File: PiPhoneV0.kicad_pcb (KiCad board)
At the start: 2 copper layers, 70.5 x 117.5 mm, 50 parts, among them J1 GPIO, J2 TL040WVS03-H1263A, J3 Conn_01x15_MountingPin, SW1 SW_Push, SW10 SW_Push, SW11 SW_Push, SW12 SW_Push, SW13 SW_Push, SW14 SW_Push, SW15 SW_Push, SW16 SW_Push, SW17 SW_Push, SW18 SW_Push, SW2 SW_Push, SW3 SW_Push, SW4 SW_Push, SW5 SW_Push, SW6 SW_Push, SW7 SW_Push, SW8 SW_Push, SW9 SW_Push, U2 TPS61165DRV

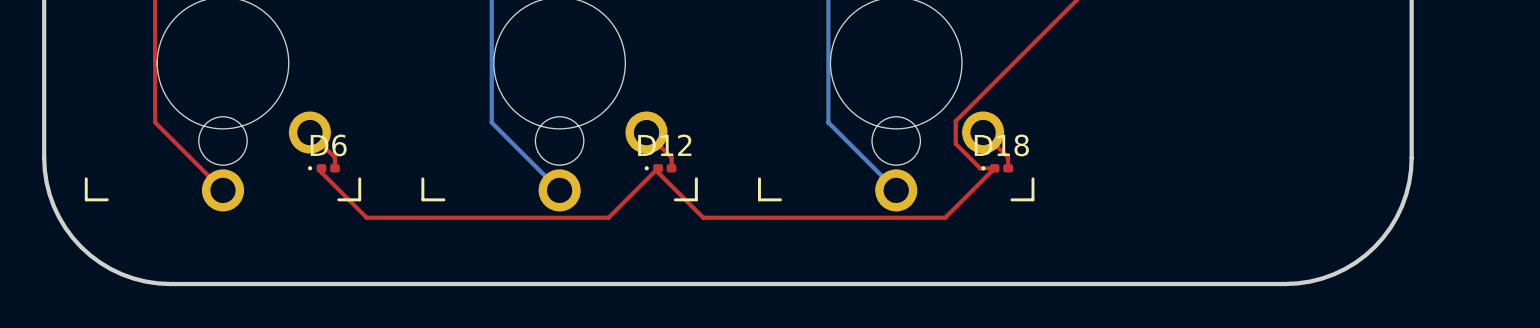
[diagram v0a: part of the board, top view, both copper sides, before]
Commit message: fix: move up bottom of the pcb
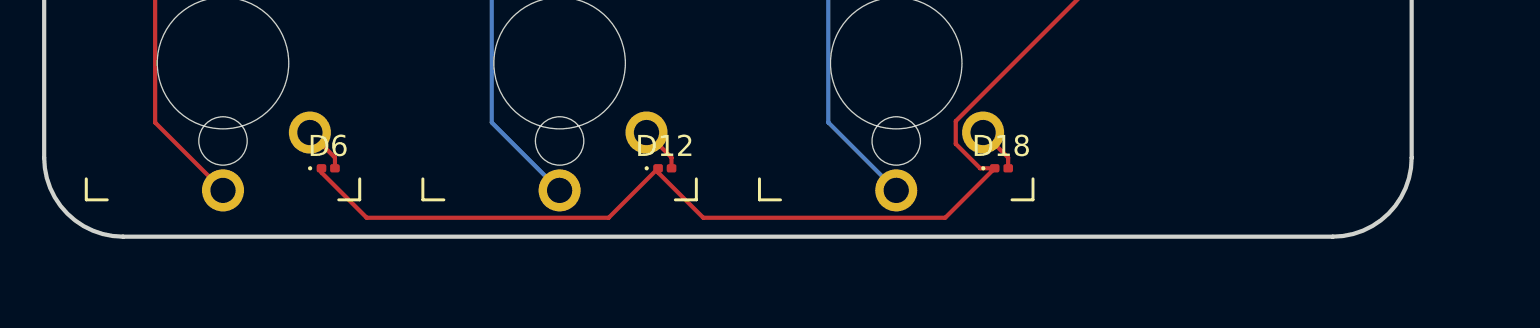
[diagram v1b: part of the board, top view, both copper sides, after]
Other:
- board size 70.5 x 117.5 mm -> 70.5 x 115.2 mm
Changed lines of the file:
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@@
+	)
+	(gr_arc
+		(start 98.25 204.25)
+		(mid 95.59835 203.15165)
+		(end 94.5 200.5)
+		(stroke
+			(width 0.2)
+			(type default)
+		)
+		(layer "Edge.Cuts")
 	)
 	(gr_arc
@@
 		(layer "Edge.Cuts")
 	)
-	(gr_arc
-		(start 159.5 200.5)
-		(mid 157.742641 204.742641)
-		(end 153.5 206.5)
-		(stroke
-			(width 0.2)
-			(type default)
-		)
-		(layer "Edge.Cuts")
-	)
-	(gr_arc
-		(start 100.5 206.5)
-		(mid 96.257359 204.742641)
-		(end 94.5 200.5)
-		(stroke
-			(width 0.2)
-			(type default)
-		)
-		(layer "Edge.Cuts")
-	)
 	(gr_line
 		(start 106 89)
@@
 	)
 	(gr_line
-		(start 100.5 206.5)
-		(end 153.5 206.5)
+		(start 155.75 204.25)
+		(end 98.25 204.25)
 		(stroke
 			(width 0.2)
+			(type default)
+		)
+		(layer "Edge.Cuts")
+	)
+	(gr_arc
+		(start 159.5 200.5)
+		(mid 158.40165 203.15165)
+		(end 155.75 204.25)
+		(stroke
+			(width 0.2)

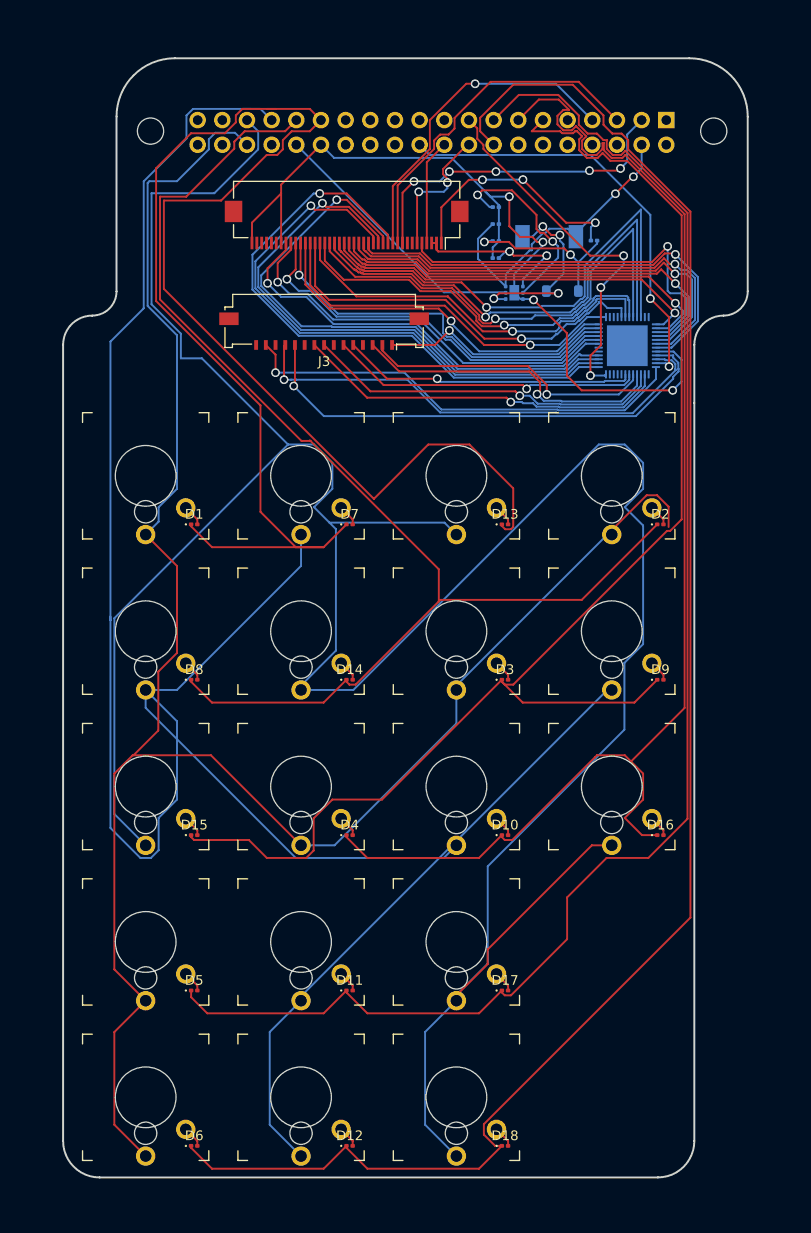
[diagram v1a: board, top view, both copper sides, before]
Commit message: feat: add ground plane, clean up keyboard wiring, move around connectors.
Note: still need to do length tuning on differential pairs and make sure
rgb signal will work ok in its current configuration.
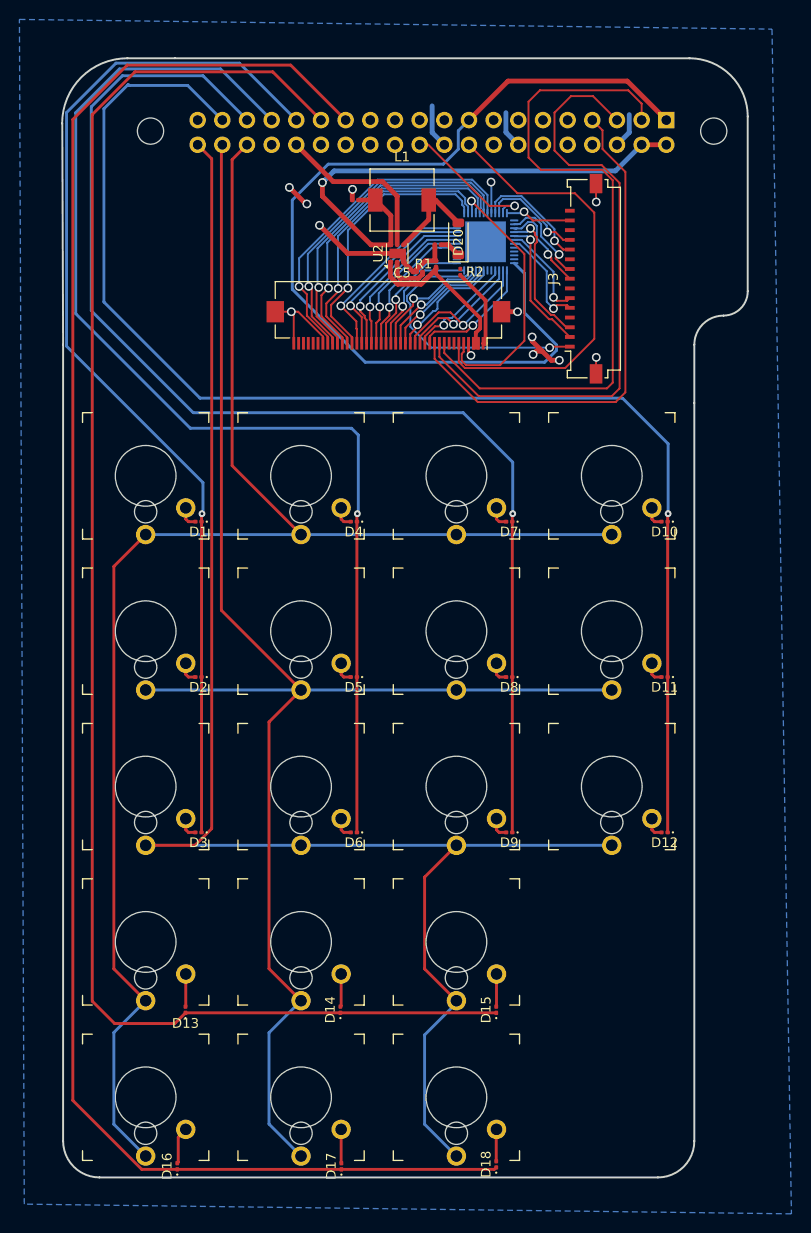
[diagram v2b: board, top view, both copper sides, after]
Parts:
- removed the D11 at (124.0, 185.0)
- removed the D12 at (124.0, 201.0)
- removed the D5 at (108.0, 185.0)
- removed the D6 at (108.0, 201.0)
- added D13: D, Diode_SMD:D_0201_0603Metric, F.Cu at (107.1, 187.0)
- added D14: D, Diode_SMD:D_0201_0603Metric, F.Cu at (123.1, 187.0)
- added D15: D, Diode_SMD:D_0201_0603Metric, F.Cu at (139.1, 187.0)
- added D16: D, Diode_SMD:D_0201_0603Metric, F.Cu at (106.3, 203.1)
- C5, C6, C7, D20, L1, R1, R2, U2: moved to F.Cu
- moved J3 26.9 mm to (147.6, 111.7), turned to 90 degrees
- moved D17 24.7 mm to (123.2, 203.1), turned to 90 degrees
- moved U1 18.1 mm to (138.0, 107.9), turned to -90 degrees
- moved L1 15.6 mm to (129.4, 103.6), turned to 0 degrees
- moved C6 14.7 mm to (124.6, 103.6), turned to 0 degrees
- moved R2 14.1 mm to (135.4, 111.0), turned to -90 degrees
- moved U2 12.7 mm to (128.9, 109.1), turned to 90 degrees
- moved D20 12.0 mm to (135.2, 107.6), turned to 90 degrees
- moved J2 11.2 mm to (128.0, 116.5)
- moved C5 10.3 mm to (131.2, 111.0), turned to 0 degrees
- moved R1 6.18 mm to (132.9, 110.2), turned to 90 degrees
- moved C7 5.97 mm to (133.1, 108.2), turned to 0 degrees
- moved D18 2.10 mm to (139.1, 202.9), turned to 90 degrees
- moved D1 0.52 mm to (108.4, 136.7), turned to 180 degrees
- moved D10 0.52 mm to (156.4, 136.7), turned to 180 degrees
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- renumbered D2 to D10, D9 to D11, D16 to D12, D8 to D2, D15 to D3, D7 to D4, D14 to D5, D4 to D6, D13 to D7, D3 to D8, D10 to D9, SW4 to SW10, SW8 to SW11, SW5 to SW2, SW9 to SW3, SW2 to SW4, SW6 to SW5, SW10 to SW6, SW3 to SW7, SW7 to SW8, SW11 to SW9
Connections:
- net Net-(J3-Pin_2) renamed /DA1N
- net Net-(J3-Pin_3) renamed /DA1P
- net Net-(J3-Pin_5) renamed /DACN
- net Net-(J3-Pin_6) renamed /DACP
- net Net-(J3-Pin_8) renamed /DA0N
- net Net-(J3-Pin_9) renamed /DA0P
- D1 pad 1: /GPIO5 -> /GPIO6
- D10 pad 1: /GPIO6 -> /GPIO26
- D11 pad 1: /GPIO17 -> /GPIO26
- D12 pad 1: /GPIO27 -> /GPIO26
- D17 pad 1: /GPIO22 -> /ID_SDA
- D18 pad 1: /GPIO23 -> /ID_SDA
- D3 pad 1: /GPIO17 -> /GPIO6
- D4 pad 1: /GPIO5 -> /GPIO13/PWM1
- D5 pad 1: /GPIO6 -> /GPIO13/PWM1
- D6 pad 1: /GPIO27 -> /GPIO13/PWM1
- D7 pad 1: /GPIO5 -> /GPIO19/PCM.FS
- D8 pad 1: /GPIO17 -> /GPIO19/PCM.FS
- D9 pad 1: /GPIO27 -> /GPIO19/PCM.FS
- J2 pad 16: Net-(J2-DB0) -> /Blue0
- J2 pad 17: Net-(J2-DB1) -> /Blue1
- J2 pad 18: Net-(J2-DB2) -> /Blue2
- J2 pad 19: Net-(J2-DB3) -> /Blue3
- J2 pad 20: Net-(J2-DB4) -> /Blue4
- J2 pad 21: Net-(J2-DB5) -> /Blue5
- J2 pad 22: Net-(J2-DB6) -> /Green0
- J2 pad 23: Net-(J2-DB7) -> /Green1
- J2 pad 24: Net-(J2-DB8) -> /Green2
- J2 pad 25: Net-(J2-DB9) -> /Green3
- J2 pad 26: Net-(J2-DB10) -> /Green4
- J2 pad 27: Net-(J2-DB11) -> /Green5
- J2 pad 28: Net-(J2-DB12) -> /Red0
- J2 pad 29: Net-(J2-DB13) -> /Red1
- J2 pad 30: Net-(J2-DB14) -> /Red2
- J2 pad 31: Net-(J2-DB15) -> /Red3
- J2 pad 32: Net-(J2-DB16) -> /Red4
- J2 pad 33: Net-(J2-DB17) -> /Red5
- J2 pad MP: unconnected-(J2-MountPin-PadMP) -> GND
- J3 pad MP: unconnected-(J3-MountPin-PadMP) -> GND
- SW11 pad 1: /GPIO13/PWM1 -> /GPIO20/PCM.DIN
- SW12 pad 1: /GPIO19/PCM.FS -> /GPIO21/PCM.DOUT
- SW14 pad 1: /GPIO13/PWM1 -> /GPIO20/PCM.DIN
- SW15 pad 1: /GPIO19/PCM.FS -> /GPIO21/PCM.DOUT
- SW15 pad 2: Net-(D17-A) -> Net-(D15-A)
- SW17 pad 1: /GPIO13/PWM1 -> /GPIO20/PCM.DIN
- SW17 pad 2: Net-(D12-A) (its old number) -> Net-(D17-A)
- SW18 pad 1: /GPIO19/PCM.FS -> /GPIO21/PCM.DOUT
- SW2 pad 1: /GPIO13/PWM1 -> /GPIO20/PCM.DIN
- SW3 pad 1: /GPIO19/PCM.FS -> /GPIO21/PCM.DOUT
- SW4 pad 1: /GPIO13/PWM1 -> /GPIO16
- SW5 pad 1: /GPIO19/PCM.FS -> /GPIO20/PCM.DIN
- SW6 pad 1: /GPIO16 -> /GPIO21/PCM.DOUT
- SW7 pad 1: /GPIO19/PCM.FS -> /GPIO16
- SW8 pad 1: /GPIO16 -> /GPIO20/PCM.DIN
- SW9 pad 1: /GPIO13/PWM1 -> /GPIO21/PCM.DOUT
- U1 pad 1: Net-(J2-DB5) -> /Red0
- U1 pad 2: Net-(J2-DB4) -> /Red1
- U1 pad 31: Net-(J2-DB17) -> /Blue0
- U1 pad 32: Net-(J2-DB16) -> /Blue1
- U1 pad 33: Net-(J2-DB15) -> /Blue2
- U1 pad 34: Net-(J2-DB14) -> /Blue3
- U1 pad 36: Net-(J2-DB13) -> /Blue4
- U1 pad 37: Net-(J2-DB12) -> /Blue5
- U1 pad 4: Net-(J2-DB3) -> /Red2
- U1 pad 41: Net-(J2-DB11) -> /Green0
- U1 pad 42: Net-(J2-DB10) -> /Green1
- U1 pad 43: Net-(J2-DB9) -> /Green2
- U1 pad 44: Net-(J2-DB8) -> /Green3
- U1 pad 45: Net-(J2-DB7) -> /Green4
- U1 pad 46: Net-(J2-DB6) -> /Green5
- U1 pad 5: Net-(J2-DB2) -> /Red3
- U1 pad 6: Net-(J2-DB1) -> /Red4
- U1 pad 7: Net-(J2-DB0) -> /Red5
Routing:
- net /ID_SDA: track 0.00 -> 180.4 mm
- net /GPIO23: track 175.3 -> 0.00 mm
- net /GPIO19/PCM.FS: track 298.7 -> 128.3 mm, vias 0 -> 1
- net /GPIO21/PCM.DOUT: track 0.00 -> 164.0 mm
- net /GPIO20/PCM.DIN: track 0.00 -> 161.0 mm
- net /GPIO22: track 155.9 -> 0.00 mm
- net /GPIO17: track 140.2 -> 0.00 mm
- net /GPIO26: track 0.00 -> 138.8 mm, vias 0 -> 1
- net /GPIO27: track 135.0 -> 0.00 mm
- net /GPIO13/PWM1: track 242.4 -> 120.4 mm, vias 0 -> 1
- net +3V3: track 38.6 -> 97.2 mm, vias 3 -> 0
- net Net-(J2-DB6): track 51.3 -> 0.00 mm, vias 1 -> 0
- net Net-(J2-DB7): track 50.6 -> 0.00 mm, vias 1 -> 0
- net Net-(J2-DB8): track 50.1 -> 0.00 mm, vias 1 -> 0
- net Net-(J2-PCLK): track 62.6 -> 12.7 mm
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- added copper zone on B.Cu, net GND
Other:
- board size 70.5 x 115.2 mm -> 70.6 x 115.2 mm
- board text removed: "Extend PCB edge 0.5mm if using SMT header"
- board text removed: "PoE"

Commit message: chore: tune length of diferential pairs
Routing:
- net /ID_SDA: track 180.4 -> 179.6 mm
- net /DA1N: track 13.7 -> 14.4 mm
- net /DACP: track 9.99 -> 10.6 mm
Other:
- board size 70.6 x 115.2 mm -> 70.5 x 115.3 mm

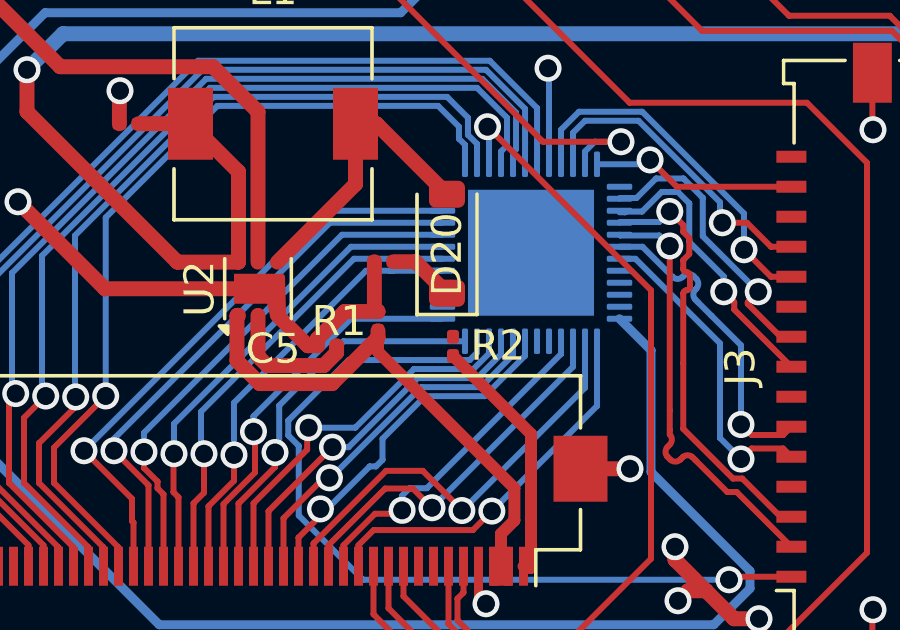
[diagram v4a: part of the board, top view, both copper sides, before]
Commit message: chore: match components with jlpcb
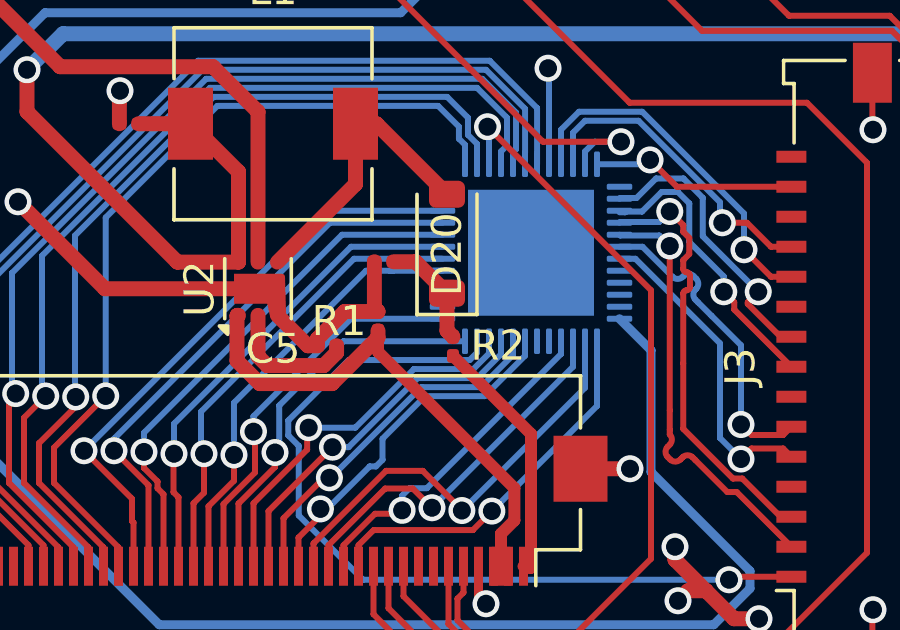
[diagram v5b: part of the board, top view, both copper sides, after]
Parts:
- U1: value ~ -> ICN6211
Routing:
- net Net-(D20-K): track 2.21 -> 3.75 mm
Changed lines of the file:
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@@
 			)
 		)
-		(property "Value" "~"
+		(property "Value" "ICN6211"
 			(at 0 -4.33 90)
 			(layer "B.Fab")
@@
 		(width 0.5)
 		(layer "F.Cu")
+		(net 102)
+	)
+	(segment
+		(start 135.2 110.5)
+		(end 135.4 110.7)
+		(width 0.5)
+		(layer "F.Cu")
+		(net 102)
+	)
+	(segment
+		(start 135.2 109.25)
+		(end 135.2 110.5)
+		(width 0.5)
+		(layer "F.Cu")

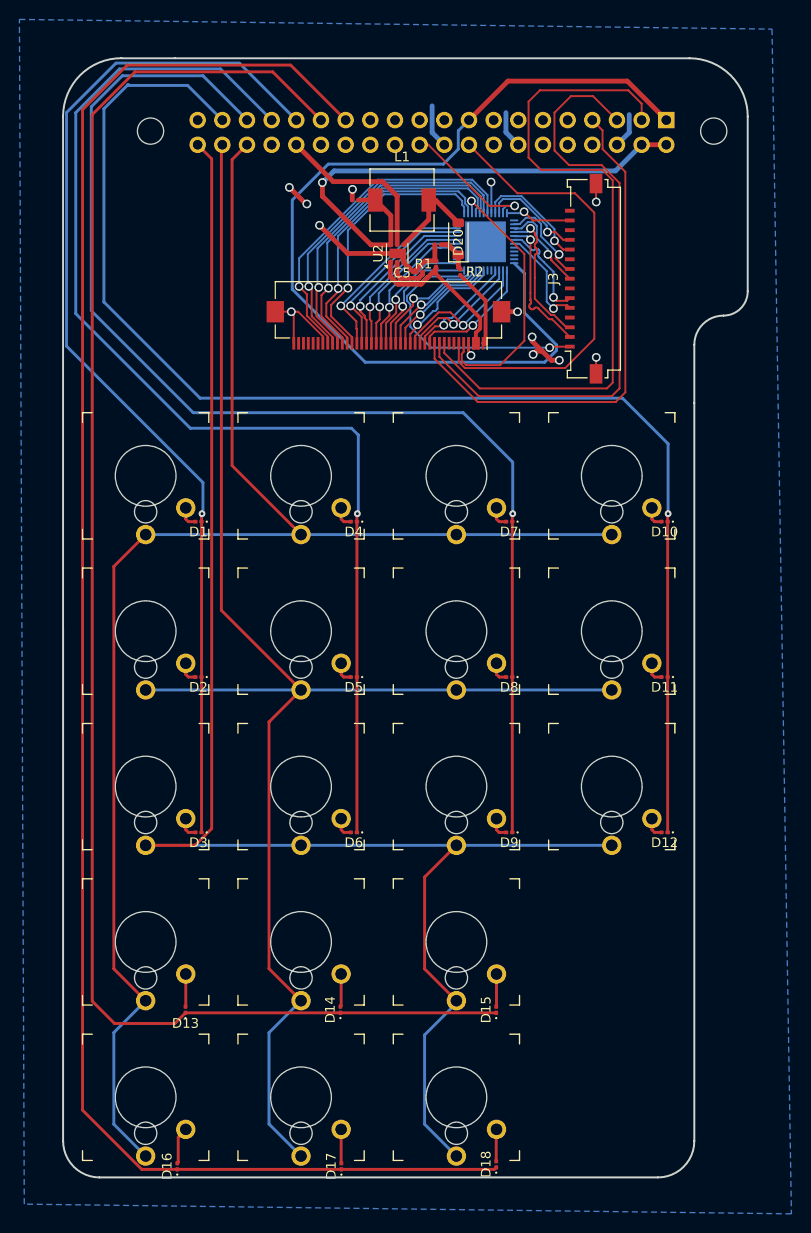
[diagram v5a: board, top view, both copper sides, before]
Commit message: feat: update adapters to match those easily on jlpcb
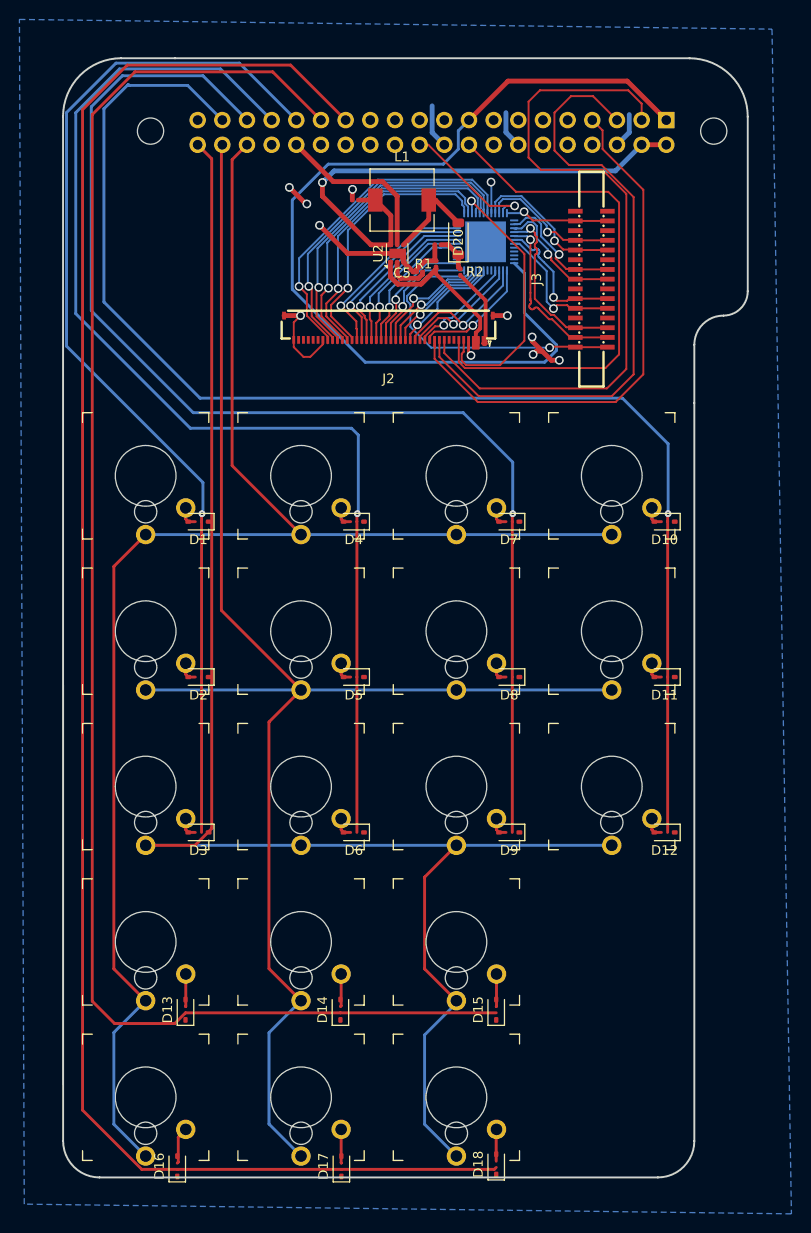
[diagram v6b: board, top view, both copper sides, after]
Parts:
- D1, D10, D11, D12, D13, D14, D15, D16, D17, D18, D2, D3, D4, D5, D6, D7, D8, D9: footprint Diode_SMD:D_0201_0603Metric -> Diode_SMD:D_SOD-323
- J2: value TL040WVS03-H1263A -> Conn_01x40_MountingPin; footprint Connector_FFC-FPC:Hirose_FH12-40S-0.5SH_1x40-1MP_P0.50mm_Horizontal -> EasyEDA:CONN-SMD_40P-P0.50_HCTL_HC-FPC-05-09-40RLTAG
- J3: footprint Connector_FFC-FPC:Molex_200528-0150_1x15-1MP_P1.00mm_Horizontal -> EasyEDA:FPC-SMD_15P-P1.00_HDGC_1.0K-GT-15PB
- moved J3 1.31 mm to (148.9, 111.8)
- moved J2 0.25 mm to (128.0, 116.8)
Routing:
- net /GPIO24: track 46.2 -> 52.8 mm
- net GND: track 56.1 -> 52.0 mm, vias 13 -> 11
- net /DA0N: track 9.62 -> 12.9 mm
- net Net-(J3-Pin_14): track 6.91 -> 10.2 mm
- net Net-(J3-Pin_12): track 10.6 -> 13.9 mm
- net Net-(J3-Pin_11): track 12.1 -> 15.4 mm
- net Net-(J3-Pin_1): track 28.3 -> 31.6 mm
- net /DACP: track 10.6 -> 13.9 mm
- net /DACN: track 10.6 -> 13.9 mm
- net /DA1P: track 14.5 -> 17.8 mm
- net /DA0P: track 9.68 -> 13.0 mm
- net /DA1N: track 14.4 -> 17.7 mm
- net /GPIO4/GPCLK0: track 53.3 -> 54.9 mm
- net /GPIO3/SCL1: track 63.3 -> 64.5 mm
- net /GPIO2/SDA1: track 70.7 -> 71.9 mm
